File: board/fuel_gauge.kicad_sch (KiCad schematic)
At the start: 3 parts, among them U701 MAX17260SETD+

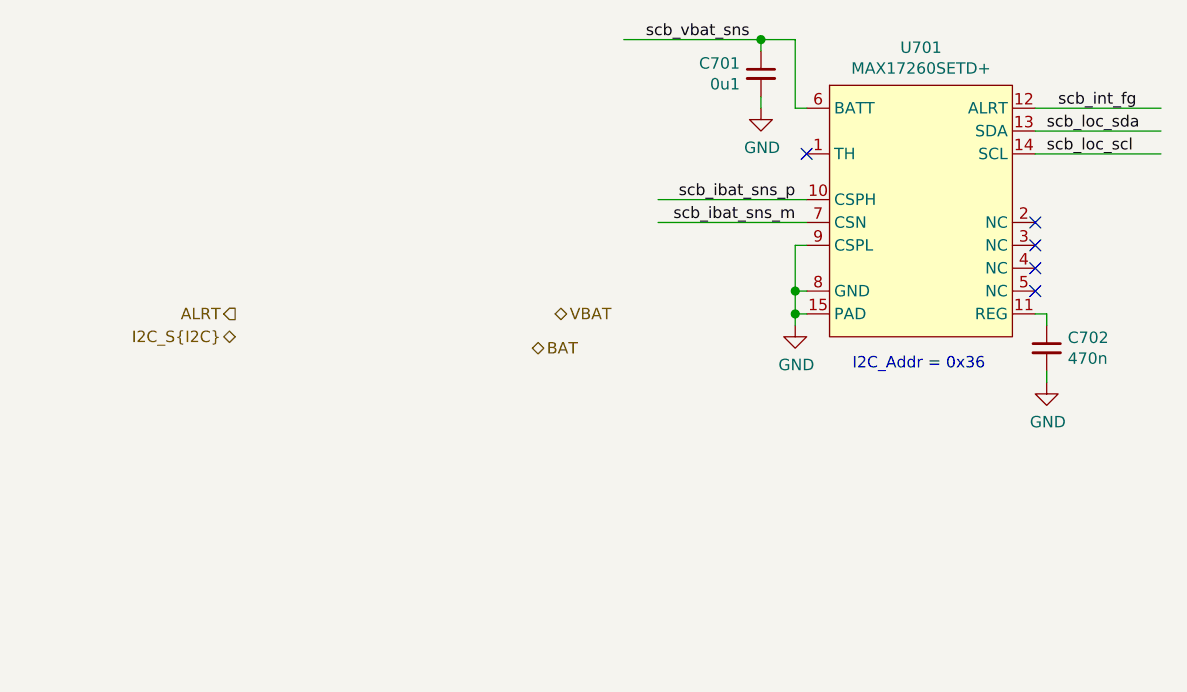
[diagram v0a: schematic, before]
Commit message: Added testpoints and other fixes
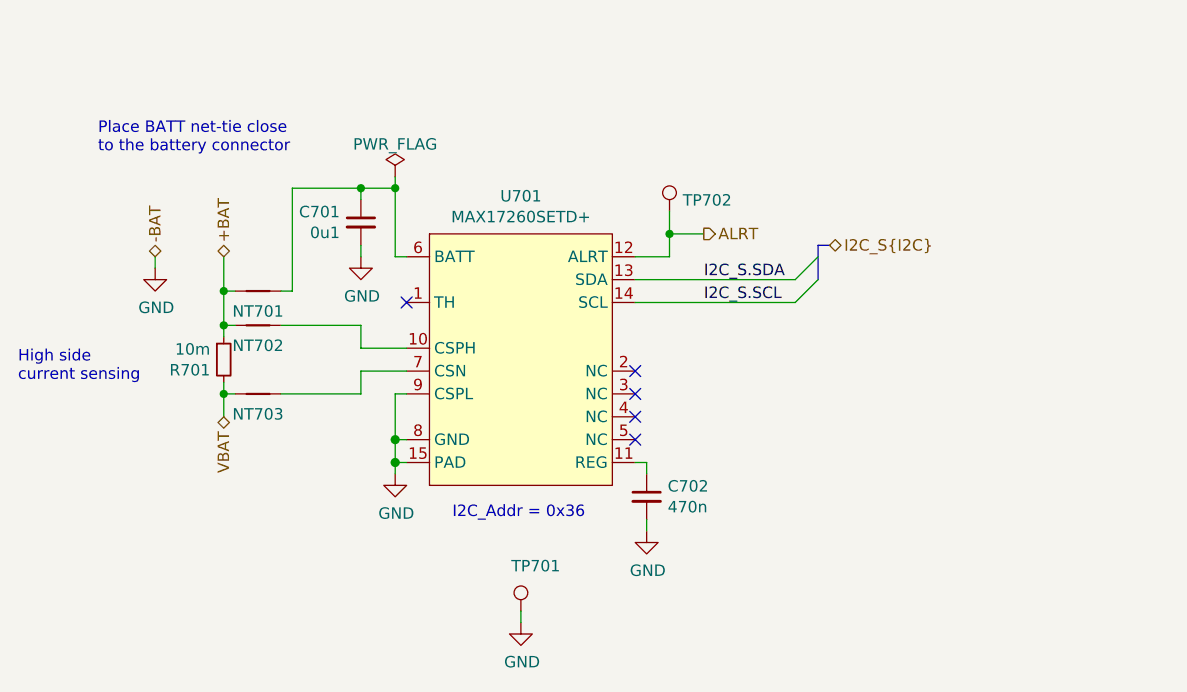
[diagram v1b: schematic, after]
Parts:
- added NT701, NT702, NT703: Net-Tie_2, symbol Device:Net-Tie_2
- added R701: 10m, symbol Device:R_Small
- added TP701, TP702: TestPoint, DIYPie:TestPoint_Pad_D1.5mm, symbol DIYPie:TestPoint
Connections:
- net scb_int_fg is gone; now on net ALRT: U701.12 (ALRT)
- net ALRT: now also TP702.1
- net GND: now also TP701.1
- net VBAT: now also NT703.2, R701.2
- net scb_ibat_sns_m: no longer names the net of U701.7 (CSN)
- net scb_ibat_sns_m: now also NT703.1
- net scb_ibat_sns_p: no longer names the net of U701.10 (CSPH)
- net scb_ibat_sns_p: now also NT702.1
- net scb_loc_scl renamed I2C_S.SCL
- net scb_loc_sda renamed I2C_S.SDA
- net scb_vbat_sns: no longer names the net of C701.1, U701.6 (BATT)
- net scb_vbat_sns: now also NT701.1
- new net +BAT: NT701.2, NT702.2, R701.1
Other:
- note added: "High side current sensing"
- note added: "Place BATT net-tie close to the battery connector"
- moved on the sheet: C701, C702, U701
